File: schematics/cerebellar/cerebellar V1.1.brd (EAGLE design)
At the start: 98.4 x 91.1 mm, 69 parts, among them CON1 ODRV2, CON2 ODRV1, CON3 ODRV3, CON4 ODRV4, CON5 ODRV5, CON6 ODRV6, IC3 LTC7001, P1 Foot1, P11 Foot2, P12 Foot3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

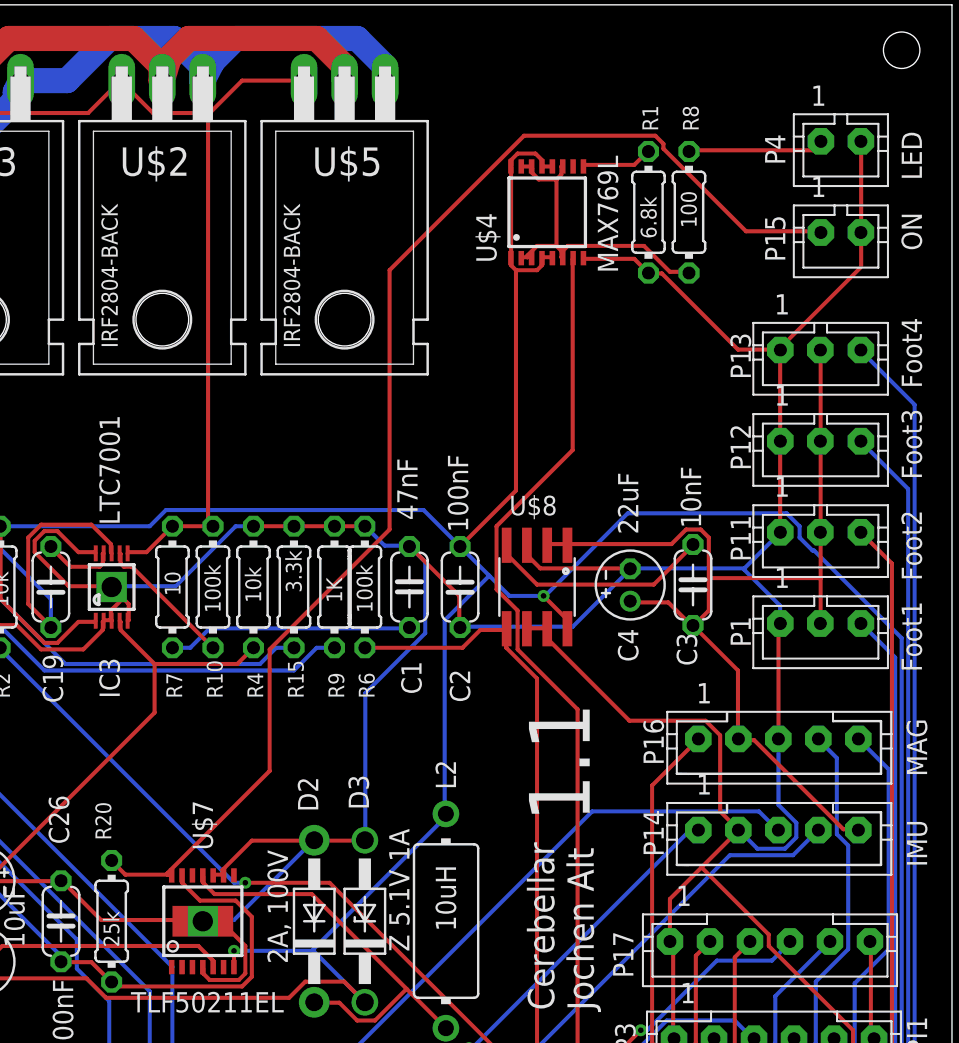
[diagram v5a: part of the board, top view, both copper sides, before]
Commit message: Added LED Power Manager
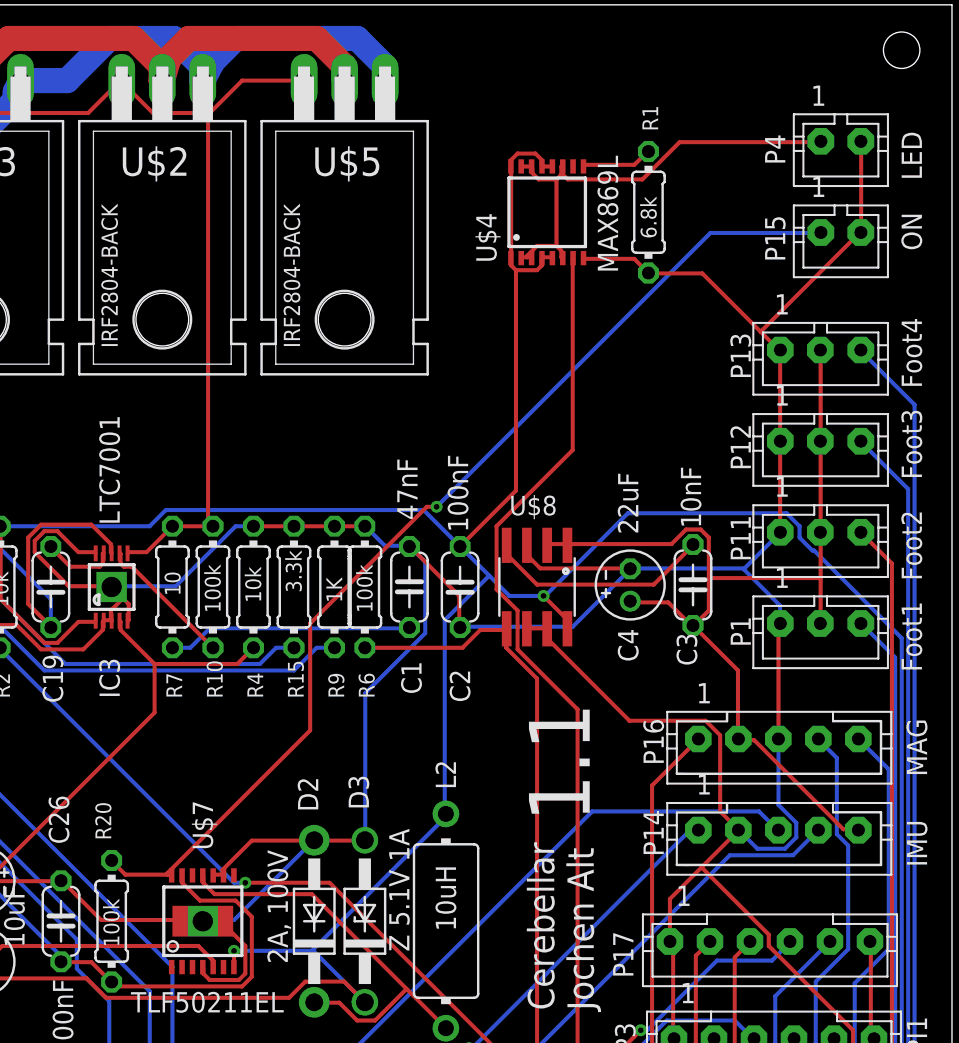
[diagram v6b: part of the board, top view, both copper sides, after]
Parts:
- removed R8: 100, rcl:0204/7
- R20: value 25k -> 100k
- U$4: value MAX769L -> MAX869L
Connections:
- net N$47 renamed SWTCH
- removed net N$3: P4.1, R8.2
- removed net N$6: R8.1, U$4.11, U$4.14, U$4.15, U$4.2, U$4.3, U$4.6
- new net LED+: P4.1, U$4.11, U$4.14, U$4.15, U$4.2, U$4.3, U$4.6
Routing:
- net LED+: track 0.00 -> 29.2 mm
- net N$6: track 20.6 -> 0.00 mm
- net SWTCH: track 81.1 -> 65.8 mm, vias 0 -> 1
- net N$3: track 8.57 -> 0.00 mm
- net GND: track 460.7 -> 460.0 mm
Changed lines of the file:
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@@
 <attribute name="VALUE" x="50.165" y="29.21" size="1.27" layer="21" rot="R180"/>
 </element>
-<element name="R20" library="rcl" library_urn="urn:adsk.eagle:library:334" package="0204/7" package3d_urn="urn:adsk.eagle:package:23498/2" value="25k" x="39.37" y="33.655" smashed="yes" rot="R90">
+<element name="R20" library="rcl" library_urn="urn:adsk.eagle:library:334" package="0204/7" package3d_urn="urn:adsk.eagle:package:23498/2" value="100k" x="39.37" y="33.655" smashed="yes" rot="R90">
 <attribute name="NAME" x="39.3446" y="38.735" size="0.9906" layer="25" ratio="10" rot="R90"/>
 <attribute name="POPULARITY" value="79" x="39.37" y="33.655" size="1.778" layer="27" rot="R90" display="off"/>
@@
 <attribute name="VALUE" x="89.2251" y="40.02" size="1.27" layer="21" rot="R270"/>
 </element>
-<element name="U$4" library="MAX869" package="TSSOP-16" value="MAX769L" x="66.675" y="78.105" smashed="yes" rot="R90">
+<element name="U$4" library="MAX869" package="TSSOP-16" value="MAX869L" x="66.675" y="78.105" smashed="yes" rot="R90">
 <attribute name="NAME" x="63.5" y="74.93" size="1.27" layer="25" rot="R90"/>
 <attribute name="VALUE" x="71.12" y="74.295" size="1.27" layer="21" rot="R90"/>
@@
 <attribute name="NAME" x="80.3351" y="83.01" size="1.27" layer="25" rot="R270"/>
 <attribute name="VALUE" x="88.9" y="83.185" size="1.27" layer="21" rot="R270"/>
-</element>
-<element name="R8" library="rcl" library_urn="urn:adsk.eagle:library:334" package="0204/7" package3d_urn="urn:adsk.eagle:package:23498/2" value="100" x="75.565" y="78.105" smashed="yes" rot="R90">
-<attribute name="NAME" x="76.1746" y="83.185" size="0.9906" layer="25" ratio="10" rot="R90"/>
-<attribute name="POPULARITY" value="79" x="75.565" y="78.105" size="1.778" layer="27" rot="R90" display="off"/>
-<attribute name="SPICEPREFIX" value="R" x="75.565" y="78.105" size="1.778" layer="27" rot="R90" display="off"/>
-<attribute name="VALUE" x="76.0476" y="77.1144" size="0.9906" layer="21" ratio="10" rot="R90"/>
 </element>
 <element name="U$8" library="LT1763" package="SO08" value="LT1763" x="66.04" y="54.61" smashed="yes" rot="R180">
@@
 <wire x1="81.28" y1="69.3928" x2="81.296" y2="69.469" width="0.254" layer="1"/>
 <wire x1="81.28" y1="63.8048" x2="81.296" y2="63.754" width="0.254" layer="1"/>
-<wire x1="73.8632" y1="74.2696" x2="73.0504" y2="74.2696" width="0.254" layer="1"/>
-<wire x1="78.6384" y1="69.4944" x2="73.8632" y2="74.2696" width="0.254" layer="1"/>
-<wire x1="81.1784" y1="69.4944" x2="78.6384" y2="69.4944" width="0.254" layer="1"/>
+<wire x1="76.4032" y1="74.2696" x2="73.0504" y2="74.2696" width="0.254" layer="1"/>
+<wire x1="81.1784" y1="69.4944" x2="80.0608" y2="70.612" width="0.254" layer="1"/>
+<wire x1="80.0608" y1="70.612" x2="76.4032" y2="74.2696" width="0.254" layer="1"/>
 <wire x1="73.0504" y1="74.2696" x2="73.025" y2="74.295" width="0.254" layer="1"/>
 <wire x1="81.1784" y1="69.4944" x2="81.296" y2="69.469" width="0.254" layer="1"/>
@@
 <wire x1="71.9328" y1="55.7784" x2="71.882" y2="55.753" width="0.254" layer="16"/>
 <wire x1="81.28" y1="58.0136" x2="81.296" y2="58.039" width="0.254" layer="16"/>
-<wire x1="86.36" y1="74.676" x2="86.36" y2="76.708" width="0.254" layer="1"/>
-<wire x1="81.28" y1="69.596" x2="86.36" y2="74.676" width="0.254" layer="1"/>
-<wire x1="86.36" y1="76.708" x2="86.344" y2="76.835" width="0.254" layer="1"/>
-<wire x1="81.28" y1="69.596" x2="81.296" y2="69.469" width="0.254" layer="1"/>
+<wire x1="80.0608" y1="70.612" x2="86.2584" y2="76.8096" width="0.254" layer="1"/>
+<wire x1="86.2584" y1="76.8096" x2="86.344" y2="76.835" width="0.254" layer="1"/>
 <wire x1="81.28" y1="53.4416" x2="81.28" y2="52.324" width="0.254" layer="16"/>
 <wire x1="79.0448" y1="55.6768" x2="81.28" y2="53.4416" width="0.254" layer="16"/>
@@
 <wire x1="45.72" y1="30.7848" x2="45.735" y2="30.78" width="0.254" layer="1"/>
 </signal>
-<signal name="N$47">
+<signal name="SWTCH">
 <contactref element="U$7" pad="14"/>
 <contactref element="P15" pad="1"/>
@@
 <wire x1="43.0784" y1="36.576" x2="43.135" y2="36.53" width="0.254" layer="1"/>
 <wire x1="39.4208" y1="37.3888" x2="39.37" y2="37.465" width="0.254" layer="1"/>
-<wire x1="79.1464" y1="76.9112" x2="83.82" y2="76.9112" width="0.254" layer="1"/>
-<wire x1="73.9648" y1="82.0928" x2="79.1464" y2="76.9112" width="0.254" layer="1"/>
-<wire x1="73.9648" y1="82.3976" x2="73.9648" y2="82.0928" width="0.254" layer="1"/>
-<wire x1="73.4568" y1="82.9056" x2="73.9648" y2="82.3976" width="0.254" layer="1"/>
-<wire x1="65.2272" y1="82.9056" x2="73.4568" y2="82.9056" width="0.254" layer="1"/>
-<wire x1="56.7944" y1="74.4728" x2="65.2272" y2="82.9056" width="0.254" layer="1"/>
-<wire x1="56.7944" y1="58.2168" x2="56.7944" y2="74.4728" width="0.254" layer="1"/>
-<wire x1="49.276" y1="50.6984" x2="56.7944" y2="58.2168" width="0.254" layer="1"/>
-<wire x1="49.276" y1="43.0784" x2="49.276" y2="50.6984" width="0.254" layer="1"/>
-<wire x1="42.8752" y1="36.6776" x2="49.276" y2="43.0784" width="0.254" layer="1"/>
-<wire x1="83.82" y1="76.9112" x2="83.836" y2="76.835" width="0.254" layer="1"/>
+<wire x1="76.9112" y1="76.8096" x2="83.82" y2="76.8096" width="0.254" layer="16"/>
+<wire x1="59.7408" y1="59.6392" x2="76.9112" y2="76.8096" width="0.254" layer="16"/>
+<wire x1="59.1312" y1="59.6392" x2="59.7408" y2="59.6392" width="0.254" layer="1"/>
+<wire x1="51.816" y1="52.324" x2="59.1312" y2="59.6392" width="0.254" layer="1"/>
+<wire x1="51.816" y1="45.6184" x2="51.816" y2="52.324" width="0.254" layer="1"/>
+<wire x1="42.8752" y1="36.6776" x2="51.816" y2="45.6184" width="0.254" layer="1"/>
+<wire x1="83.82" y1="76.8096" x2="83.836" y2="76.835" width="0.254" layer="16"/>
 <wire x1="42.8752" y1="36.6776" x2="42.8752" y2="36.576" width="0.254" layer="1"/>
+<via x="59.7408" y="59.6392" extent="1-16" drill="0.35"/>
 </signal>
 <signal name="SCK">
@@
 <wire x1="72.9488" y1="81.8896" x2="73.025" y2="81.915" width="0.254" layer="1"/>
 </signal>
-<signal name="N$6">
+<signal name="LED+">
 <contactref element="U$4" pad="6"/>
 <contactref element="U$4" pad="11"/>
@@
 <contactref element="U$4" pad="2"/>
 <contactref element="U$4" pad="15"/>
-<contactref element="R8" pad="1"/>
+<contactref element="P4" pad="1"/>
 <wire x1="65.6336" y1="75.2856" x2="65.4304" y2="75.2856" width="0.254" layer="1"/>
 <wire x1="65.4304" y1="75.2856" x2="65.1256" y2="75.2856" width="0.254" layer="1"/>
@@
 <wire x1="65.7352" y1="80.8736" x2="65.7" y2="80.98" width="0.254" layer="1"/>
 <wire x1="67.2592" y1="80.1624" x2="67.2592" y2="75.9968" width="0.254" layer="1"/>
-<wire x1="74.3712" y1="74.3712" x2="75.4888" y2="74.3712" width="0.254" layer="1"/>
-<wire x1="72.7456" y1="75.9968" x2="74.3712" y2="74.3712" width="0.254" layer="1"/>
-<wire x1="67.9704" y1="75.9968" x2="72.7456" y2="75.9968" width="0.254" layer="1"/>
-<wire x1="67.6656" y1="75.692" x2="67.9704" y2="75.9968" width="0.254" layer="1"/>
-<wire x1="75.4888" y1="74.3712" x2="75.565" y2="74.295" width="0.254" layer="1"/>
-<wire x1="67.6656" y1="75.692" x2="67.564" y2="75.692" width="0.254" layer="1"/>
-</signal>
-<signal name="N$3">
-<contactref element="R8" pad="2"/>
-<contactref element="P4" pad="1"/>
-<wire x1="83.312" y1="81.9912" x2="75.5904" y2="81.9912" width="0.254" layer="1"/>
-<wire x1="83.82" y1="82.4992" x2="83.312" y2="81.9912" width="0.254" layer="1"/>
-<wire x1="75.5904" y1="81.9912" x2="75.565" y2="81.915" width="0.254" layer="1"/>
+<wire x1="74.9808" y1="82.4992" x2="83.82" y2="82.4992" width="0.254" layer="1"/>
+<wire x1="72.644" y1="80.1624" x2="74.9808" y2="82.4992" width="0.254" layer="1"/>
+<wire x1="67.9704" y1="80.1624" x2="72.644" y2="80.1624" width="0.254" layer="1"/>
+<wire x1="67.6656" y1="80.4672" x2="67.9704" y2="80.1624" width="0.254" layer="1"/>
 <wire x1="83.82" y1="82.4992" x2="83.836" y2="82.55" width="0.254" layer="1"/>
+<wire x1="67.6656" y1="80.4672" x2="67.564" y2="80.4672" width="0.254" layer="1"/>
 </signal>
 <signal name="MAG_SCL">

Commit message: improved schmeatics
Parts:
- moved LED1 61.3 mm to (64.1, 52.1)
- moved C3 25.6 mm to (72.6, 80.1)
- moved C4 16.7 mm to (69.3, 71.2)
- moved U$8 16.1 mm to (63.5, 70.5)
- moved LED3 8.26 mm to (5.08, 68.6)
- moved SJ5 4.49 mm to (17.1, 74.9)
- moved P14 4.45 mm to (77.5, 39.4)
- moved P15 4.45 mm to (80.6, 76.8)
- moved P16 4.45 mm to (77.5, 45.1)
- moved P3 4.45 mm to (76.5, 26.3)
- moved P4 4.45 mm to (80.6, 82.5)
- moved SJ1 4.45 mm to (17.1, 80.6)
- moved SJ2 4.45 mm to (17.1, 83.2)
- moved SJ3 4.45 mm to (17.1, 71.8), turned to 180 degrees
- moved P1 4.44 mm to (79.4, 50.8)
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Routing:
- net N$39: track 57.6 -> 12.9 mm
- net SENS3: track 112.6 -> 89.8 mm, vias 0 -> 3
- net GND: track 460.0 -> 482.7 mm, vias 0 -> 3
- net TXD: track 54.7 -> 76.2 mm, vias 1 -> 0
- net PMS+: track 74.9 -> 95.0 mm, vias 0 -> 1
- net O2_RX: track 49.2 -> 69.3 mm, vias 1 -> 0
- net POWER+: track 140.3 -> 121.5 mm, vias 0 -> 1
- net SHDN: track 42.5 -> 61.2 mm, vias 0 -> 1
- net O5_TX: track 81.5 -> 99.6 mm, vias 1 -> 0
- net MISO1: track 49.3 -> 65.2 mm, vias 0 -> 1
- net MOSI: track 38.7 -> 25.9 mm
- net LED_PWM: track 59.6 -> 72.3 mm, vias 0 -> 3
- net O6_RX: track 51.1 -> 63.6 mm
- net O2_TX: track 47.7 -> 59.9 mm
- net TS: track 52.2 -> 64.4 mm
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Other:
- board size 98.4 x 91.1 mm -> 95.9 x 90.5 mm

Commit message: started Raspi
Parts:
- moved C2 16.6 mm to (68.8, 68.6)
- moved C3 13.4 mm to (65.7, 68.7)
- moved R1 13.4 mm to (62.9, 68.6)
- moved C4 10.5 mm to (59.2, 68.7)
- moved U$8 9.94 mm to (59.1, 79.4)
- moved LED1 6.98 mm to (64.1, 45.1)
- moved U$4 6.35 mm to (69.8, 80.0)
- moved C1 4.26 mm to (54.9, 50.8)
- moved C19 4.26 mm to (32.4, 50.8)
- moved IC3 4.26 mm to (36.2, 50.8)
- moved R10 4.26 mm to (42.5, 50.8)
- moved R15 4.26 mm to (47.6, 50.8)
- moved R4 4.26 mm to (45.1, 50.8)
- moved R6 4.26 mm to (52.1, 50.8)
- moved R9 4.26 mm to (50.2, 50.8)
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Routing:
- net GND: track 482.7 -> 0.00 mm, vias 3 -> 0
- net +5V: track 254.2 -> 0.00 mm, vias 4 -> 0
- net POWER+: track 121.5 -> 0.00 mm, vias 1 -> 0
- net N$17: track 120.8 -> 0.00 mm, vias 1 -> 0
- net SENS4: track 113.7 -> 0.00 mm, vias 2 -> 0
- net O5_TX: track 99.6 -> 0.00 mm
- net PMS+: track 95.0 -> 0.00 mm, vias 1 -> 0
- net BATT-: track 90.9 -> 0.00 mm
- net SENS3: track 89.8 -> 0.00 mm, vias 3 -> 0
- net O5_RX: track 89.2 -> 0.00 mm, vias 2 -> 0
- net N$22: track 81.6 -> 0.00 mm, vias 4 -> 0
- net O1_RX: track 80.1 -> 0.00 mm
- net O1_TX: track 79.3 -> 0.00 mm
- net TXD: track 76.2 -> 0.00 mm
- net LED_PWM: track 72.3 -> 0.00 mm, vias 3 -> 0
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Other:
- board size 95.9 x 90.5 mm -> 94.6 x 90.5 mm
